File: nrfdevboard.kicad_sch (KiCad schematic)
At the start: 15 parts, among them J1 USB2.0, J3 Conn_01x17_Pin, J4 Conn_01x17_Pin, U1 MDBT50Q-P1MV2, Y1 32.768

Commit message: Finished p1
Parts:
- J1: footprint TH-A1OC:th_pogo_pins_4 -> Connector_USB:USB_A_Kycon_KUSBX-AS1N-B_Horizontal
- J3: footprint (none) -> Connector_Samtec_HPM_THT:Samtec_HPM-17-01-x-S_Straight_1x17_Pitch5.08mm
- J4: footprint (none) -> Connector_Samtec_HPM_THT:Samtec_HPM-17-01-x-S_Straight_1x17_Pitch5.08mm; symbol Connector:Conn_01x17_Pin -> nrfdevboard:Conn_01x17_Pin
- U1: footprint TH-A1OC:TH_MDBT50Q-P1MV2 -> TH1:TH_MDBT50Q-P1MV2
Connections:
- net 0.04/AIN2: now also J4.10 (Pin_10); no longer J4.2 (Pin_2)
- net 0.05/AIN3: now also J4.7 (Pin_7); no longer J4.3 (Pin_3)
- net 0.13: now also J3.11 (Pin_11); no longer J3.17 (Pin_17)
- net 0.17: now also J3.10 (Pin_10); no longer J3.14 (Pin_14)
- net 0.19: now also J3.14 (Pin_14); no longer J3.13 (Pin_13)
- net 0.20: now also J3.9 (Pin_9); no longer J3.11 (Pin_11)
- net 0.21: now also J3.13 (Pin_13); no longer J3.12 (Pin_12)
- net 0.22: now also J3.8 (Pin_8); no longer J3.9 (Pin_9)
- net 0.23: now also J3.12 (Pin_12); no longer J3.10 (Pin_10)
- net 0.24: now also J3.7 (Pin_7); no longer J3.8 (Pin_8)
- net 0.25: now also J3.6 (Pin_6); no longer J3.7 (Pin_7)
- net 0.26: now also J4.8 (Pin_8); no longer J4.1 (Pin_1)
- net 3v3: now also J3.4 (Pin_4); no longer J3.5 (Pin_5)
- net D+: no longer J1.3 (D+), R2.1
- net D-: no longer J1.2 (D-), R3.1
- net GND: now also J3.1 (Pin_1), J3.5 (Pin_5), J4.1 (Pin_1), J4.14 (Pin_14), J4.16 (Pin_16), J4.17 (Pin_17); no longer J3.2 (Pin_2), J3.6 (Pin_6), J4.11 (Pin_11)
- net SWDCLK: now also J3.2 (Pin_2); no longer J3.3 (Pin_3)
- net SWDIO: now also J3.3 (Pin_3); no longer J3.4 (Pin_4)
- net VBUS_USB: now also J3.17 (Pin_17)
- net at U1.12 (P0.31_LF/AIN7): no longer J4.17 (Pin_17)
- net at U1.13 (P0.28_LF/AIN4): no longer J4.16 (Pin_16)
- net 0.30/AIN6: now reaches U1.14 (P0.30/AIN6)
- net 0.30/AIN6: now also J4.2 (Pin_2)
- net 0.27: now reaches U1.16 (P0.27)
- net 0.27: now also J4.9 (Pin_9); no longer J4.14 (Pin_14)
- net 0.06: now reaches U1.22 (P0.06)
- net 0.06: now also J4.11 (Pin_11); no longer J4.4 (Pin_4)
- net 0.07/TRCLK: now reaches U1.23 (P0.07/TRACECLK)
- net 0.07/TRCLK: now also J4.6 (Pin_6); no longer J4.5 (Pin_5)
- net 0.08: now reaches U1.24 (P0.08)
- net 0.08: now also J4.12 (Pin_12); no longer J4.6 (Pin_6)
- net 1.08: now reaches U1.25 (P1.08)
- net 1.08: now also J4.5 (Pin_5); no longer J4.7 (Pin_7)
- net 1.09/TRD3: now reaches U1.26 (P1.09/TRACEDATA3)
- net 1.09/TRD3: now also J4.13 (Pin_13); no longer J4.8 (Pin_8)
- net 0.11/TRD2: now reaches U1.27 (P0.11/TRACEDATA2)
- net 0.11/TRD2: now also J4.4 (Pin_4); no longer J4.9 (Pin_9)
- net 0.12/TRD1: now reaches U1.29 (P0.12/TRACEDATA1)
- net 0.12/TRD1: now also J4.3 (Pin_3); no longer J4.10 (Pin_10)
- net at U1.52 (P0.09/NFC1): no longer J4.13 (Pin_13)
- net at U1.54 (P0.10/NFC2): no longer J4.12 (Pin_12)
- net 0.16 renamed 0.38
- net 5v renamed VBUS
- net VBUS: no longer J3.1 (Pin_1)
- net nRESET renamed 0.18/nRESET
- new net c_D+: J1.3 (D+), R2.1
- new net c_D-: J1.2 (D-), R3.1
- no-connect marks 19 -> 22
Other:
- moved on the sheet: J3, J4

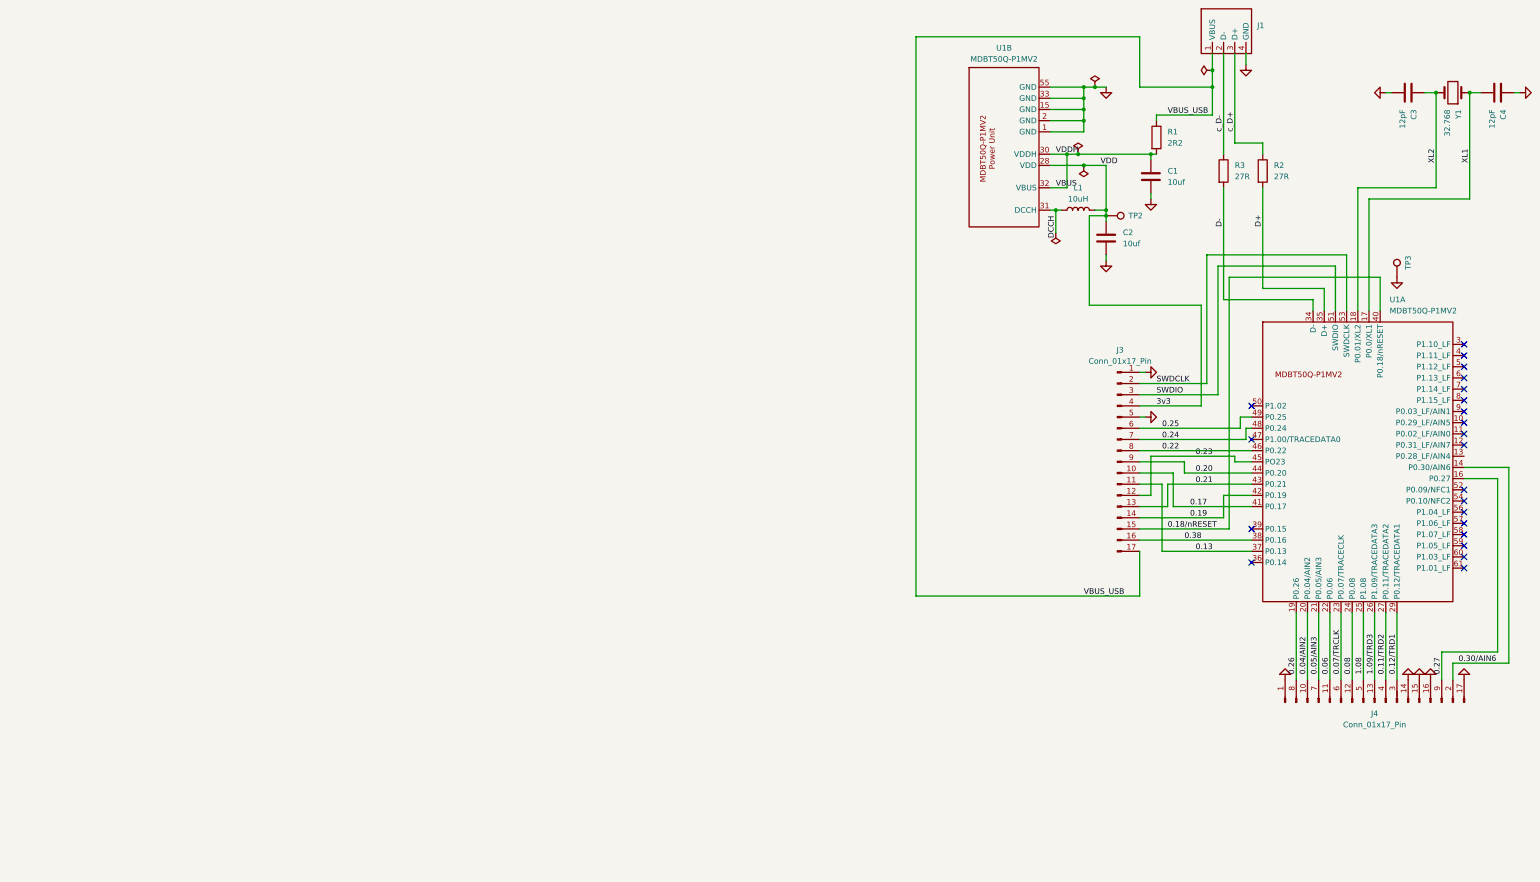
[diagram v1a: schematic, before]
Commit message: PDBv2: Redesign for a framework module
V2 brings two main changes. Firstly the size has been greatly reduced to
fit into a framework module. With only 7 pins now.

Additionally, v1 had issues when running from 5v USB. I am still not
sure what this issue is since its identical to the datasheet, but I'm
now including an external voltage regulator to run the chip at 3v3. This
also reduces the BOM.
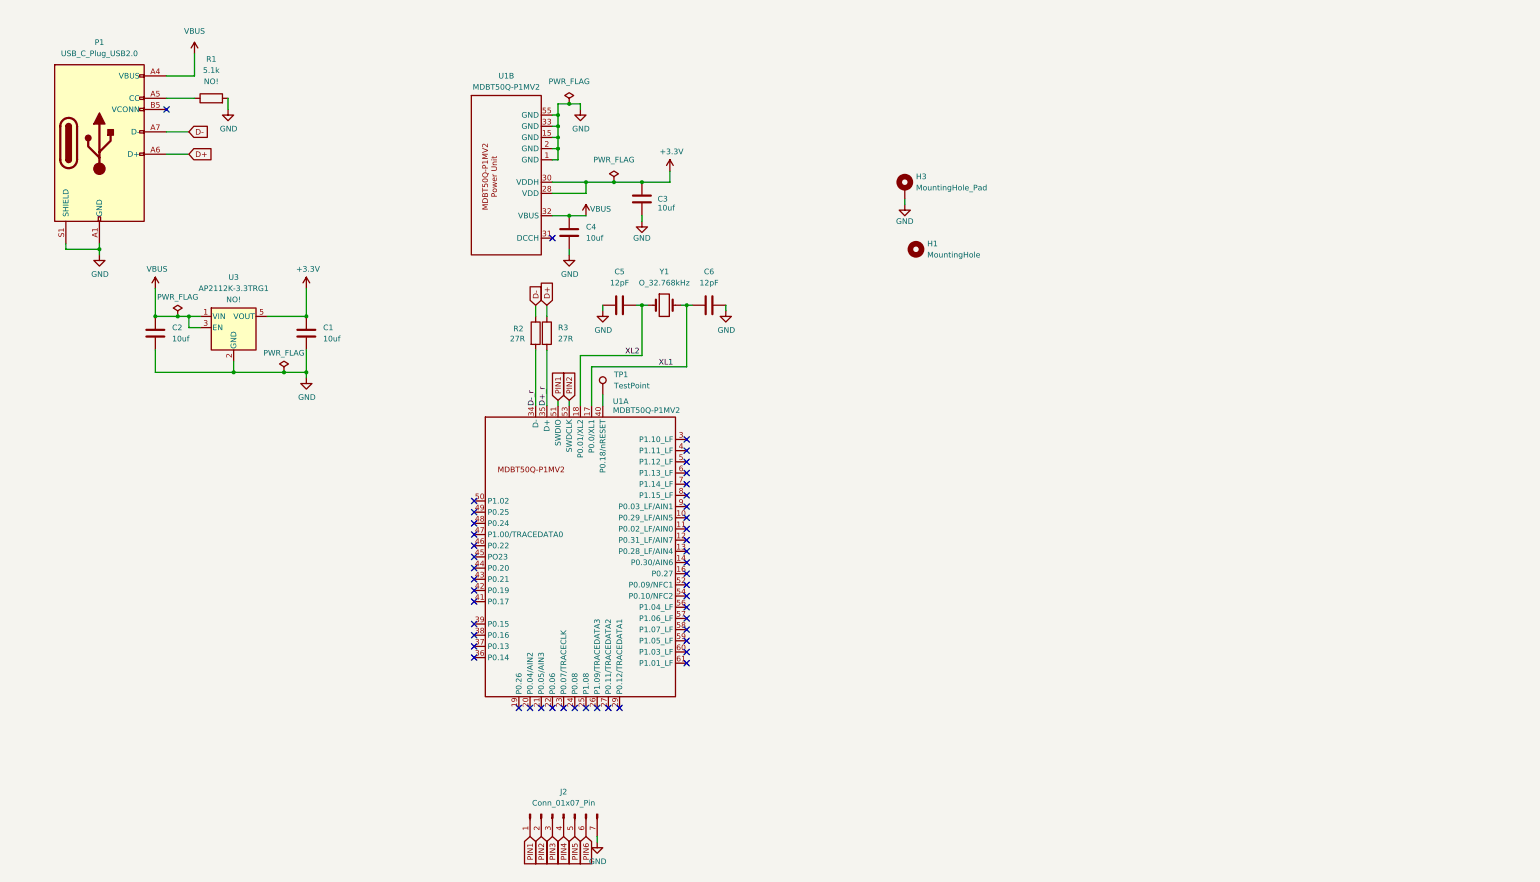
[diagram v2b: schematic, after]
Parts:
- removed C1, C2: 10uf, Capacitor_SMD:C_0805_2012Metric, symbol Device:C
- removed C3, C4: 12pF, Capacitor_SMD:C_0603_1608Metric, symbol Device:C
- removed J1: USB2.0, Connector_USB:USB_A_Kycon_KUSBX-AS1N-B_Horizontal, symbol TH-A10C:USB2_POGO_4
- removed J3: Conn_01x17_Pin, Connector_Samtec_HPM_THT:Samtec_HPM-17-01-x-S_Straight_1x17_Pitch5.08mm, symbol Connector:Conn_01x17_Pin
- removed J4: Conn_01x17_Pin, Connector_Samtec_HPM_THT:Samtec_HPM-17-01-x-S_Straight_1x17_Pitch5.08mm, symbol nrfdevboard:Conn_01x17_Pin
- removed L1: 10uH, Inductor_SMD:L_0603_1608Metric, symbol Device:L
- removed R1: 2R2, Resistor_SMD:R_0603_1608Metric, symbol Device:R
- removed R2, R3: 27R, Resistor_SMD:R_0603_1608Metric, symbol Device:R
- removed TP2, TP3: TestPoint, TestPoint:TestPoint_Pad_D2.0mm, symbol Connector:TestPoint
- removed U1: MDBT50Q-P1MV2, TH1:TH_MDBT50Q-P1MV2, symbol TH-A10C:MDBT50Q-P1MV2
- removed Y1: 32.768, Crystal:Crystal_SMD_3215-2Pin_3.2x1.5mm, symbol Device:Crystal
- added C1, C2, C3, C4: 10uf, Capacitor_SMD:C_0805_2012Metric, symbol TH-1-CC:C_10uf
- added C5, C6: 12pF, Capacitor_SMD:C_0603_1608Metric, symbol TH-1-CC:C_12pf
- added H1: MountingHole, MountingHole:MountingHole_2.2mm_M2, symbol Mechanical:MountingHole
- added H3: MountingHole_Pad, MountingHole:MountingHole_2.2mm_M2_Pad, symbol Mechanical:MountingHole_Pad
- added J2: Conn_01x07_Pin, TH-1-CC:7_side_pin, symbol Connector:Conn_01x07_Pin
- added P1: USB_C_Plug_USB2.0, symbol Connector:USB_C_Plug_USB2.0
- added R1: 5.1k, Resistor_SMD:R_0603_1608Metric, symbol TH-1-CC:R_5.1k
- added R2, R3: 27R, Resistor_SMD:R_0603_1608Metric, symbol TH-1-CC:R_27Ω
- added TP1: TestPoint, TestPoint:TestPoint_Pad_D1.0mm, symbol Connector:TestPoint
- added U1: MDBT50Q-P1MV2, TH-1-CC_footprints:TH_MDBT50Q-P1MV2, symbol TH-1-CC:MDBT50Q-P1MV2
- added U3: AP2112K-3.3TRG1, Package_TO_SOT_SMD:SOT-23-5, symbol TH-1-CC:AP2112K-3.3
- added Y1: O_32.768kHz, Crystal:Crystal_SMD_3215-2Pin_3.2x1.5mm, symbol TH-1-CC:O_32.768kHz
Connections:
- net D+: now also P1.A6 (D+), R3.1
- net D-: now also P1.A7 (D-), R2.1
- net GND: now also C1.2, C2.2, C3.2, C4.2, C5.1, C6.2, H3.1, J2.7 (Pin_7), P1.A1 (GND), P1.A12 (GND), P1.B1 (GND), P1.B12 (GND), P1.S1 (SHIELD), R1.2, U1.1 (GND), U1.15 (GND), U1.2 (GND), U1.33 (GND), U1.55 (GND), U3.2 (GND)
- net VBUS: now also C2.1, C4.1, P1.A4 (VBUS), P1.A9 (VBUS), P1.B4 (VBUS), P1.B9 (VBUS), U1.32 (VBUS), U3.1 (VIN), U3.3 (EN)
- net XL1: now also C6.1, U1.17 (P0.0/XL1), Y1.2
- net XL2: now also C5.2, U1.18 (P0.01/XL2), Y1.1
- new net: TP1.1, U1.40 (P0.18/nRESET)
- new net: P1.A5 (CC), R1.1
- new net +3.3V: C1.1, C3.1, U1.28 (VDD), U1.30 (VDDH), U3.5 (VOUT)
- new net D+_r: R3.2, U1.35 (D+)
- new net D-_r: R2.2, U1.34 (D-)
- new net PIN1: J2.1 (Pin_1), U1.51 (SWDIO)
- new net PIN2: J2.2 (Pin_2), U1.53 (SWDCLK)
- new net PIN3: J2.3 (Pin_3)
- new net PIN4: J2.4 (Pin_4)
- new net PIN5: J2.5 (Pin_5)
- new net PIN6: J2.6 (Pin_6)
- no-connect marks 22 -> 47

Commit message: Minor tweaks
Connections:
- net CC: now reaches P1.A5 (CC), R1.1
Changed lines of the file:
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@@
+		)
+	)
+	(label "CC"
+		(at 54.61 43.18 0)
+		(effects
+			(font
+				(size 1.27 1.27)
+			)
+			(justify left bottom)
 		)
 	)

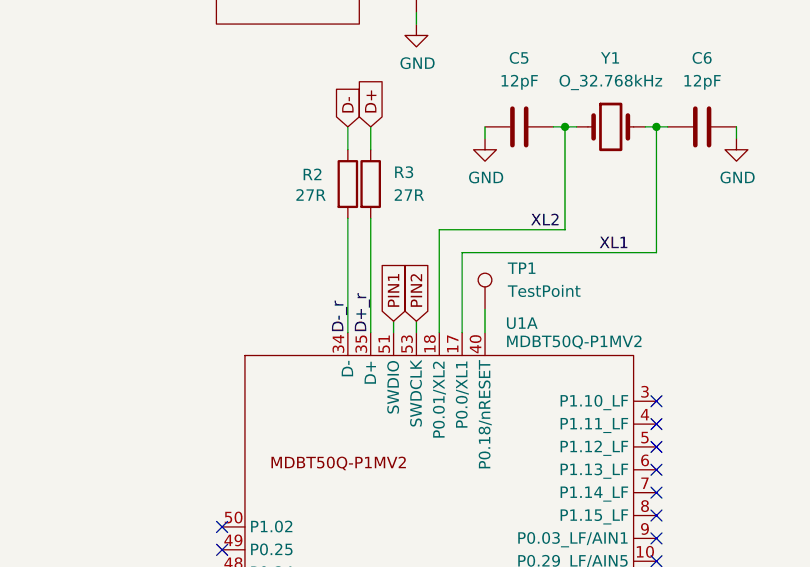
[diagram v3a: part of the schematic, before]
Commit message: Add fw expansion case and proper usbc footprint
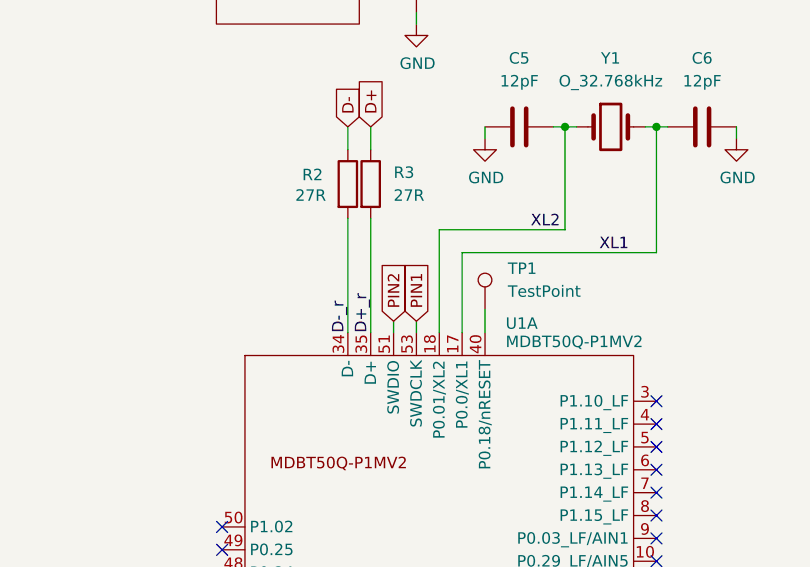
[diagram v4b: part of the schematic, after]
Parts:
- P1: footprint (none) -> TH-1-CC:USBC
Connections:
- net PIN1: now also U1.53 (SWDCLK); no longer U1.51 (SWDIO)
- net PIN2: now also U1.51 (SWDIO); no longer U1.53 (SWDCLK)
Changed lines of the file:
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@@
 	(global_label "PIN2"
 		(shape input)
-		(at 143.51 111.76 90)
+		(at 140.97 111.76 90)
 		(fields_autoplaced yes)
 		(effects
@@
 		)
 		(property "Intersheetrefs" "${INTERSHEET_REFS}"
-			(at 143.51 104.7191 90)
+			(at 140.97 104.7191 90)
 			(effects
 				(font
@@
 	(global_label "PIN1"
 		(shape input)
-		(at 140.97 111.76 90)
+		(at 143.51 111.76 90)
 		(fields_autoplaced yes)
 		(effects
@@
 		)
 		(property "Intersheetrefs" "${INTERSHEET_REFS}"
-			(at 140.97 104.7191 90)
+			(at 143.51 104.7191 90)
 			(effects
 				(font
@@
 			)
 		)
-		(property "Footprint" ""
+		(property "Footprint" "TH-1-CC:USBC"
 			(at 40.64 53.34 0)
 			(effects

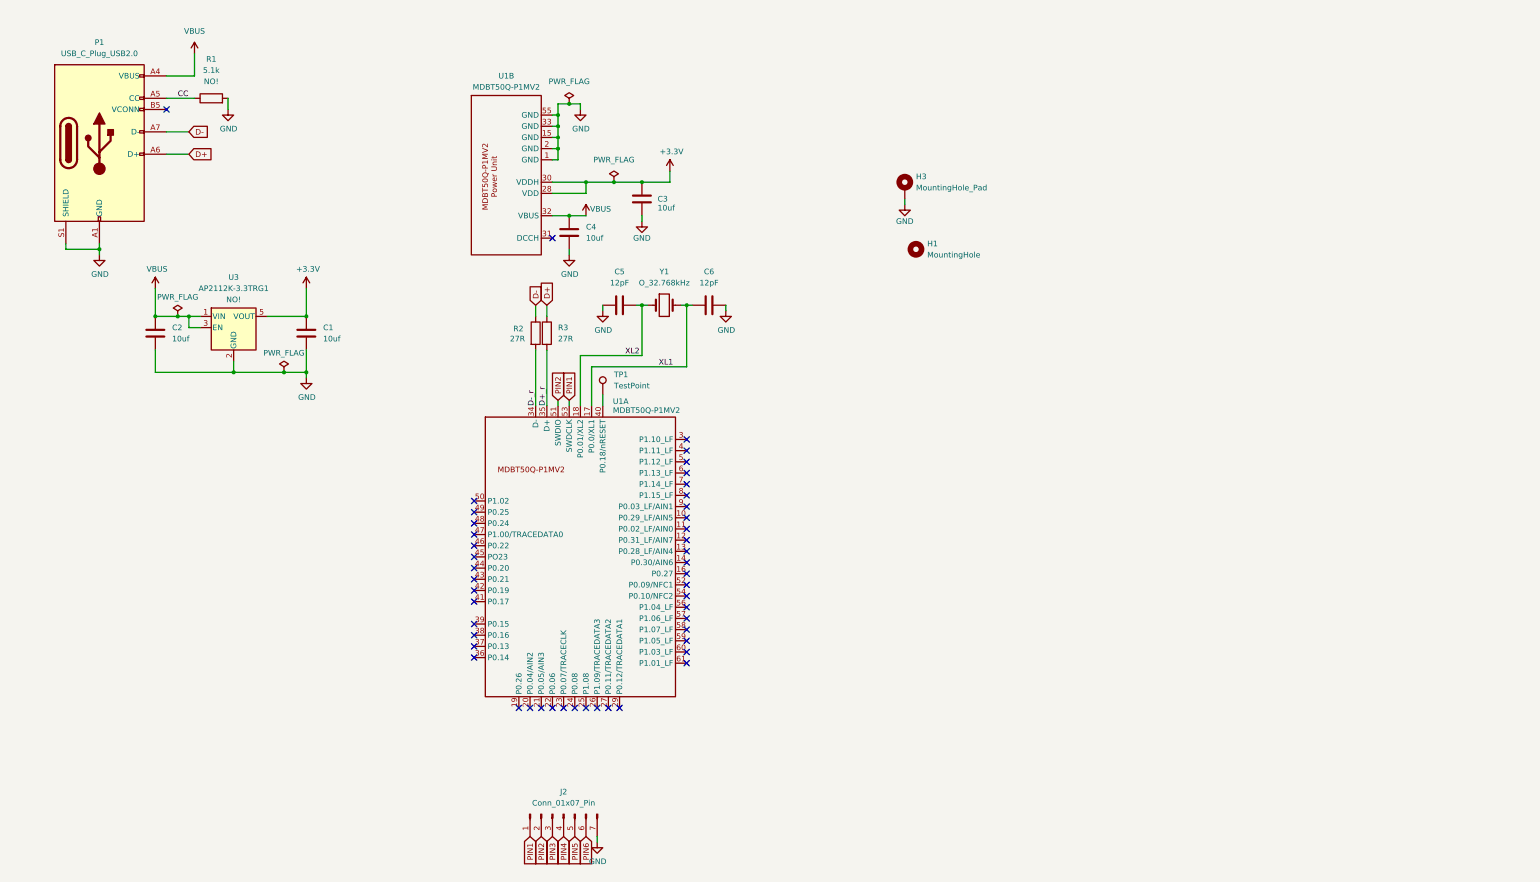
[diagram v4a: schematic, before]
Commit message: Initial routing + 7 more GPIO pins
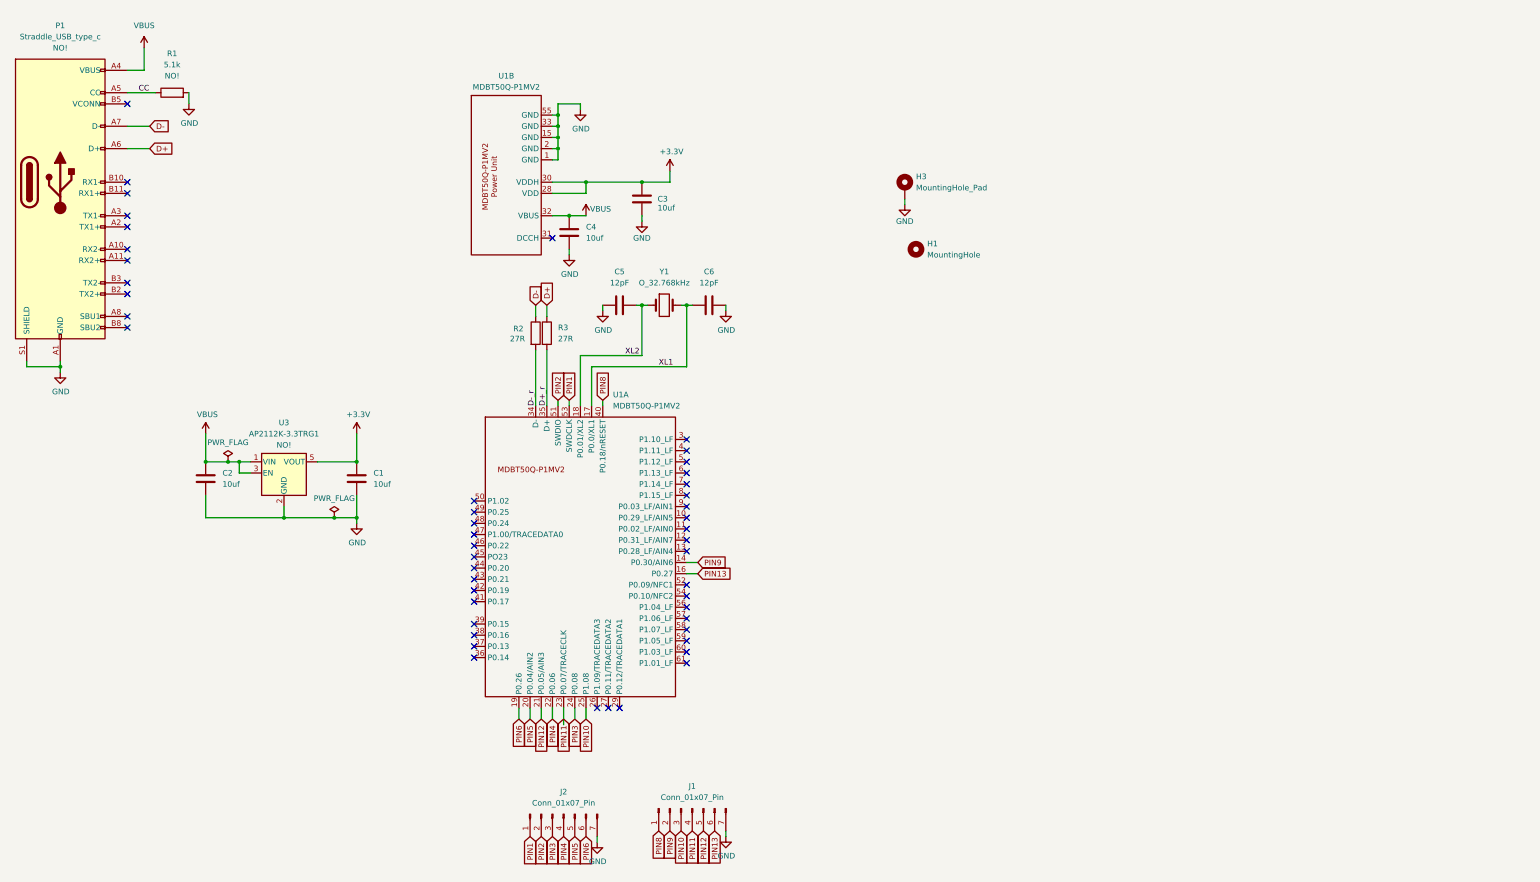
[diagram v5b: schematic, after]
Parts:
- removed P1: USB_C_Plug_USB2.0, TH-1-CC:USBC, symbol Connector:USB_C_Plug_USB2.0
- removed TP1: TestPoint, TestPoint:TestPoint_Pad_D1.0mm, symbol Connector:TestPoint
- added J1: Conn_01x07_Pin, TH-1-CC:7_side_pin, symbol Connector:Conn_01x07_Pin
- added P1: Straddle_USB_type_c, TH-1-CC_footprints:USBC, symbol TH-1-CC:Straddle_USB_type_c
- U1: footprint TH-1-CC_footprints:TH_MDBT50Q-P1MV2 -> TH-1-CC:TH_MDBT50Q-P1MV2
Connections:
- net CC: now also P1.A5 (CC)
- net D+: now also P1.A6 (D+)
- net D-: now also P1.A7 (D-)
- net GND: now also J1.7 (Pin_7), P1.A1 (GND), P1.A12 (GND), P1.B1 (GND), P1.B12 (GND), P1.S1 (SHIELD)
- net PIN3: now also U1.24 (P0.08)
- net PIN4: now also U1.22 (P0.06)
- net PIN5: now also U1.20 (P0.04/AIN2)
- net PIN6: now also U1.19 (P0.26)
- net VBUS: now also P1.A4 (VBUS), P1.A9 (VBUS), P1.B4 (VBUS), P1.B9 (VBUS)
- net PIN9: now reaches U1.14 (P0.30/AIN6)
- net PIN9: now also J1.2 (Pin_2)
- net PIN13: now reaches U1.16 (P0.27)
- net PIN13: now also J1.6 (Pin_6)
- net PIN12: now reaches U1.21 (P0.05/AIN3)
- net PIN12: now also J1.5 (Pin_5)
- net PIN11: now reaches U1.23 (P0.07/TRACECLK)
- net PIN11: now also J1.4 (Pin_4)
- net PIN10: now reaches U1.25 (P1.08)
- net PIN10: now also J1.3 (Pin_3)
- net PIN8: now reaches U1.40 (P0.18/nRESET)
- net PIN8: now also J1.1 (Pin_1)
- no-connect marks 47 -> 48
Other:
- moved on the sheet: C1, C2, R1, U3
